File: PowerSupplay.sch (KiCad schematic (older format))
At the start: 26 parts, among them J13 Jack-DC, U4 AP1117-33, U5 MC34063, U6 MC34063, U7 78M09

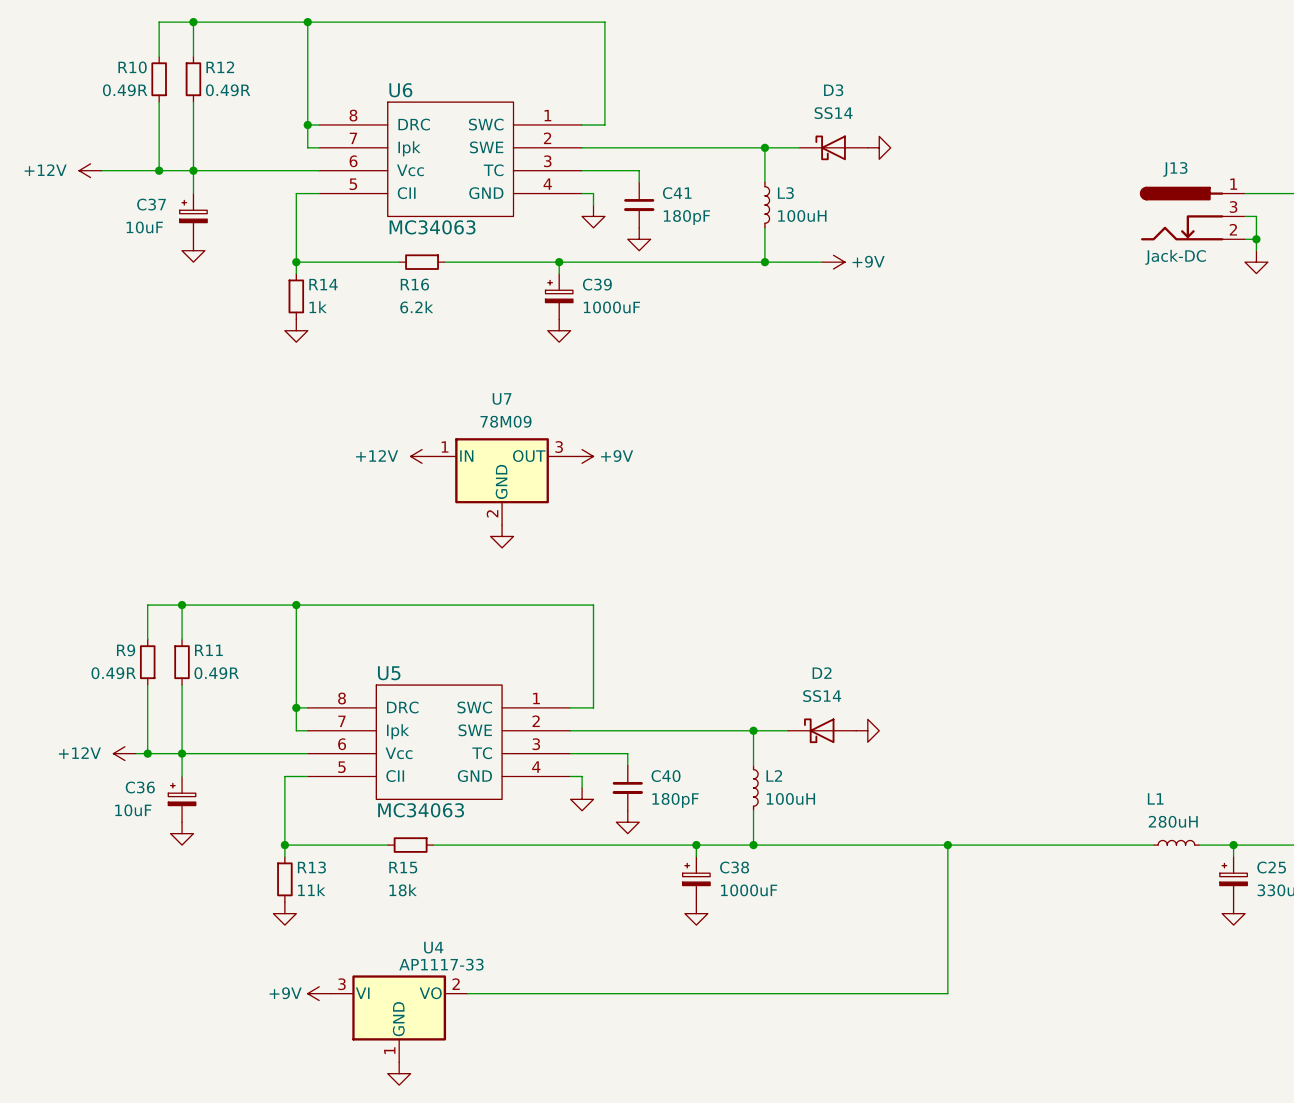
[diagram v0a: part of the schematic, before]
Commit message: TODO: power supplay connector
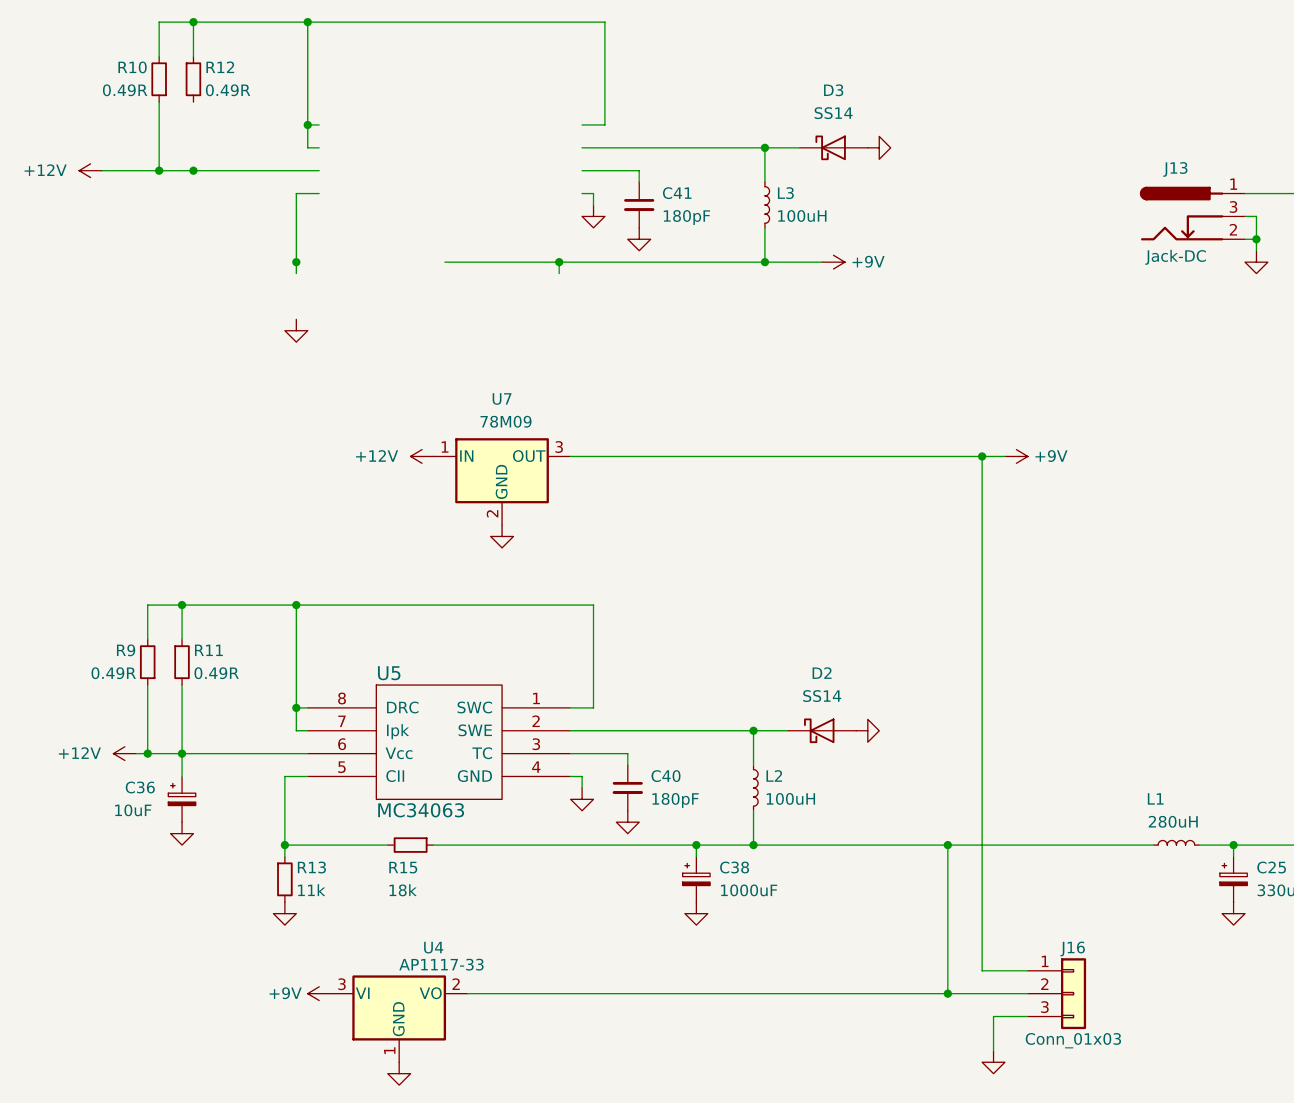
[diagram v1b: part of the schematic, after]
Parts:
- removed C37: 10uF, Capacitors_ThroughHole:CP_Radial_D4.0mm_P2.00mm, symbol CP_Small
- removed C39: 1000uF, Capacitors_ThroughHole:CP_Radial_D10.0mm_P5.00mm, symbol CP_Small
- removed R14: 1k, UI:R_1206_0603, symbol R_Small
- removed R16: 6.2k, UI:R_1206_0603, symbol R_Small
- removed U6: MC34063, UI:SOIC-8_3.9x4.9mm_Pitch1.27mm, symbol MC34063
- added J16: Conn_01x03, symbol Conn_01x03
- C36: footprint Capacitors_ThroughHole:CP_Radial_D4.0mm_P2.00mm -> Capacitors_THT:CP_Radial_D6.3mm_P2.50mm
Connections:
- wire segments 55 -> 58
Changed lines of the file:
@@
 	1250 2000 2200 2000
-Wire Wire Line
-	1650 1700 1650 2100
 Wire Wire Line
 	1650 1500 1650 1350
@@
 Wire Wire Line
 	2750 2400 4400 2400
-Wire Wire Line
-	2550 2400 2100 2400
 Connection ~ 2100 2400
 $Comp
-L GND #PWR052
+L GND #PWR68
 U 1 1 5DD9A087
 P 4600 1900
-F 0 "#PWR052" H 4600 1650 50  0001 C CNN
+F 0 "#PWR68" H 4600 1650 50  0001 C CNN
 F 1 "GND" H 4600 1750 50  0001 C CNN
 F 2 "" H 4600 1900 50  0001 C CNN
@@
 Connection ~ 3250 2400
 $Comp
-L GND #PWR053
+L GND #PWR64
 U 1 1 5DD9A371
 P 3600 2250
-F 0 "#PWR053" H 3600 2000 50  0001 C CNN
+F 0 "#PWR64" H 3600 2000 50  0001 C CNN
 F 1 "GND" H 3600 2100 50  0001 C CNN
 F 2 "" H 3600 2250 50  0001 C CNN
@@
 $EndComp
 $Comp
-L GND #PWR054
+L GND #PWR62
 U 1 1 5DD9A42B
 P 3400 2150
-F 0 "#PWR054" H 3400 1900 50  0001 C CNN
+F 0 "#PWR62" H 3400 1900 50  0001 C CNN
 F 1 "GND" H 3400 2000 50  0001 C CNN
 F 2 "" H 3400 2150 50  0001 C CNN
@@
 Connection ~ 2150 1350
 $Comp
-L +12V #PWR055
+L +12V #PWR52
 U 1 1 5DD9A4E4
 P 1250 2000
-F 0 "#PWR055" H 1250 1850 50  0001 C CNN
+F 0 "#PWR52" H 1250 1850 50  0001 C CNN
 F 1 "+12V" V 1250 2250 50  0000 C CNN
 F 2 "" H 1250 2000 50  0001 C CNN
@@
 Connection ~ 4150 2400
 $Comp
-L +12V #PWR056
+L +12V #PWR59
 U 1 1 5DD9C169
 P 2700 3250
-F 0 "#PWR056" H 2700 3100 50  0001 C CNN
+F 0 "#PWR59" H 2700 3100 50  0001 C CNN
 F 1 "+12V" V 2700 3500 50  0000 C CNN
 F 2 "" H 2700 3250 50  0001 C CNN
@@
 $EndComp
 $Comp
-L +9V #PWR057
+L +9V #PWR66
 U 1 1 5DD9C2C5
 P 4400 2400
-F 0 "#PWR057" H 4400 2250 50  0001 C CNN
+F 0 "#PWR66" H 4400 2250 50  0001 C CNN
 F 1 "+9V" V 4400 2600 50  0000 C CNN
 F 2 "" H 4400 2400 50  0001 C CNN
@@
 $EndComp
 $Comp
-L +9V #PWR058
+L +9V #PWR70
 U 1 1 5DD9C3E9
-P 3300 3250
-F 0 "#PWR058" H 3300 3100 50  0001 C CNN
-F 1 "+9V" V 3300 3450 50  0000 C CNN
-F 2 "" H 3300 3250 50  0001 C CNN
-F 3 "" H 3300 3250 50  0001 C CNN
-	1    3300 3250
+P 5200 3250
+F 0 "#PWR70" H 5200 3100 50  0001 C CNN
+F 1 "+9V" V 5200 3450 50  0000 C CNN
+F 2 "" H 5200 3250 50  0001 C CNN
+F 3 "" H 5200 3250 50  0001 C CNN
+	1    5200 3250
 	0    1    1    0
 $EndComp
 $Comp
-L GND #PWR059
+L GND #PWR60
 U 1 1 5DD9C454
 P 3000 3550
-F 0 "#PWR059" H 3000 3300 50  0001 C CNN
+F 0 "#PWR60" H 3000 3300 50  0001 C CNN
 F 1 "GND" H 3000 3400 50  0001 C CNN
 F 2 "" H 3000 3550 50  0001 C CNN
@@
 $EndComp
 $Comp
-L GND #PWR060
-U 1 1 5DD9C4CE
-P 3250 2650
-F 0 "#PWR060" H 3250 2400 50  0001 C CNN
-F 1 "GND" H 3250 2500 50  0001 C CNN
-F 2 "" H 3250 2650 50  0001 C CNN
-F 3 "" H 3250 2650 50  0001 C CNN
-	1    3250 2650
-	1    0    0    -1
-$EndComp
-$Comp
-L GND #PWR061
+L GND #PWR56
 U 1 1 5DD9C54A
 P 2100 2650
-F 0 "#PWR061" H 2100 2400 50  0001 C CNN
+F 0 "#PWR56" H 2100 2400 50  0001 C CNN
 F 1 "GND" H 2100 2500 50  0001 C CNN
 F 2 "" H 2100 2650 50  0001 C CNN
@@
 	1    0    0    -1
 $EndComp
-$Comp
-L GND #PWR062
-U 1 1 5DD9C5AC
-P 1650 2300
-F 0 "#PWR062" H 1650 2050 50  0001 C CNN
-F 1 "GND" H 1650 2150 50  0001 C CNN
-F 2 "" H 1650 2300 50  0001 C CNN
-F 3 "" H 1650 2300 50  0001 C CNN
-	1    1650 2300
-	1    0    0    -1
-$EndComp
 Wire Wire Line
 	1400 4550 2150 4550
@@
 Connection ~ 2050 4950
 $Comp
-L GND #PWR063
+L GND #PWR67
 U 1 1 5DD9C919
 P 4550 4450
-F 0 "#PWR063" H 4550 4200 50  0001 C CNN
+F 0 "#PWR67" H 4550 4200 50  0001 C CNN
 F 1 "GND" H 4550 4300 50  0001 C CNN
 F 2 "" H 4550 4450 50  0001 C CNN
@@
 	3550 4550 3550 4600
 $Comp
-L GND #PWR064
+L GND #PWR63
 U 1 1 5DD9C936
 P 3550 4800
-F 0 "#PWR064" H 3550 4550 50  0001 C CNN
+F 0 "#PWR63" H 3550 4550 50  0001 C CNN
 F 1 "GND" H 3550 4650 50  0001 C CNN
 F 2 "" H 3550 4800 50  0001 C CNN
@@
 $EndComp
 $Comp
-L GND #PWR065
+L GND #PWR61
 U 1 1 5DD9C93C
 P 3350 4700
-F 0 "#PWR065" H 3350 4450 50  0001 C CNN
+F 0 "#PWR61" H 3350 4450 50  0001 C CNN
 F 1 "GND" H 3350 4550 50  0001 C CNN
 F 2 "" H 3350 4700 50  0001 C CNN
@@
 Connection ~ 4100 4950
 $Comp
-L GND #PWR066
+L GND #PWR58
 U 1 1 5DD9C97A
 P 2550 5900
-F 0 "#PWR066" H 2550 5650 50  0001 C CNN
+F 0 "#PWR58" H 2550 5650 50  0001 C CNN
 F 1 "GND" H 2550 5750 50  0001 C CNN
 F 2 "" H 2550 5900 50  0001 C CNN
@@
 $EndComp
 $Comp
-L GND #PWR067
+L GND #PWR65
 U 1 1 5DD9C980
 P 3850 5200
-F 0 "#PWR067" H 3850 4950 50  0001 C CNN
+F 0 "#PWR65" H 3850 4950 50  0001 C CNN
 F 1 "GND" H 3850 5050 50  0001 C CNN
 F 2 "" H 3850 5200 50  0001 C CNN
@@
 $EndComp
 $Comp
-L GND #PWR068
+L GND #PWR55
 U 1 1 5DD9C98C
 P 2050 5200
-F 0 "#PWR068" H 2050 4950 50  0001 C CNN
+F 0 "#PWR55" H 2050 4950 50  0001 C CNN
 F 1 "GND" H 2050 5050 50  0001 C CNN
 F 2 "" H 2050 5200 50  0001 C CNN
@@
 $EndComp
 $Comp
-L GND #PWR069
+L GND #PWR54
 U 1 1 5DD9C992
 P 1600 4850
-F 0 "#PWR069" H 1600 4600 50  0001 C CNN
+F 0 "#PWR54" H 1600 4600 50  0001 C CNN
 F 1 "GND" H 1600 4700 50  0001 C CNN
 F 2 "" H 1600 4850 50  0001 C CNN
@@
 $EndComp
 $Comp
-L +3V3 #PWR070
+L +3V3 #PWR75
 U 1 1 5DDE50CB
 P 6800 4950
-F 0 "#PWR070" H 6800 4800 50  0001 C CNN
+F 0 "#PWR75" H 6800 4800 50  0001 C CNN
 F 1 "+3V3" V 6800 5200 50  0000 C CNN
 F 2 "" H 6800 4950 50  0001 C CNN
@@
 $EndComp
 $Comp
-L GND #PWR071
+L GND #PWR71
 U 1 1 5DDE5565
 P 6200 5200
-F 0 "#PWR071" H 6200 4950 50  0001 C CNN
+F 0 "#PWR71" H 6200 4950 50  0001 C CNN
 F 1 "GND" H 6200 5050 50  0001 C CNN
 F 2 "" H 6200 5200 50  0001 C CNN
@@
 $EndComp
 $Comp
-L GND #PWR072
+L GND #PWR74
 U 1 1 5DDE5612
 P 6700 5200
-F 0 "#PWR072" H 6700 4950 50  0001 C CNN
+F 0 "#PWR74" H 6700 4950 50  0001 C CNN
 F 1 "GND" H 6700 5050 50  0001 C CNN
 F 2 "" H 6700 5200 50  0001 C CNN
@@
 	6700 5000 6700 4950
 Connection ~ 6700 4950
-$Comp
-L MC34063 U6
-U 1 1 5DDF7FFA
-P 2800 2000
-F 0 "U6" H 2500 2350 60  0000 L CNN
-F 1 "MC34063" H 2500 1750 60  0000 L CNN
-F 2 "UI:SOIC-8_3.9x4.9mm_Pitch1.27mm" H 2700 2000 60  0001 C CNN
-F 3 "" H 2700 2000 60  0000 C CNN
-	1    2800 2000
-	1    0    0    -1
-$EndComp
 $Comp
 L MC34063 U5
@@
 $EndComp
 $Comp
-L CP_Small C39
-U 1 1 5DDF914E
-P 3250 2550
-F 0 "C39" H 3350 2600 50  0000 L CNN
-F 1 "1000uF" H 3350 2500 50  0000 L CNN
-F 2 "Capacitors_ThroughHole:CP_Radial_D10.0mm_P5.00mm" H 3250 2550 50  0001 C CNN
-F 3 "" H 3250 2550 50  0001 C CNN
-	1    3250 2550
-	1    0    0    -1
-$EndComp
-$Comp
-L R_Small R16
-U 1 1 5DDF965B
-P 2650 2400
-F 0 "R16" V 2750 2300 50  0000 L CNN
-F 1 "6.2k" V 2850 2300 50  0000 L CNN
-F 2 "UI:R_1206_0603" H 2650 2400 50  0001 C CNN
-F 3 "" H 2650 2400 50  0001 C CNN
-	1    2650 2400
-	0    1    1    0
-$EndComp
-$Comp
-L R_Small R14
-U 1 1 5DDF97A0
-P 2100 2550
-F 0 "R14" H 2150 2600 50  0000 L CNN
-F 1 "1k" H 2150 2500 50  0000 L CNN
-F 2 "UI:R_1206_0603" H 2100 2550 50  0001 C CNN
-F 3 "" H 2100 2550 50  0001 C CNN
-	1    2100 2550
-	1    0    0    -1
-$EndComp
-$Comp
-L CP_Small C37
-U 1 1 5DDF9926
-P 1650 2200
-F 0 "C37" H 1400 2250 50  0000 L CNN
-F 1 "10uF" H 1350 2150 50  0000 L CNN
-F 2 "Capacitors_ThroughHole:CP_Radial_D4.0mm_P2.00mm" H 1650 2200 50  0001 C CNN
-F 3 "" H 1650 2200 50  0001 C CNN
-	1    1650 2200
-	1    0    0    -1
-$EndComp
-$Comp
 L L_Small L3
 U 1 1 5DDFA0D4
@@
 F 0 "C36" H 1350 4800 50  0000 L CNN
 F 1 "10uF" H 1300 4700 50  0000 L CNN
-F 2 "Capacitors_ThroughHole:CP_Radial_D4.0mm_P2.00mm" H 1600 4750 50  0001 C CNN
+F 2 "Capacitors_THT:CP_Radial_D6.3mm_P2.50mm" H 1600 4750 50  0001 C CNN
 F 3 "" H 1600 4750 50  0001 C CNN
 	1    1600 4750
@@
 $EndComp
 $Comp
-L +9V #PWR073
+L +9V #PWR57
 U 1 1 5DE21DEE
 P 2250 5600
-F 0 "#PWR073" H 2250 5450 50  0001 C CNN
+F 0 "#PWR57" H 2250 5450 50  0001 C CNN
 F 1 "+9V" V 2250 5800 50  0000 C CNN
 F 2 "" H 2250 5600 50  0001 C CNN
@@
 $EndComp
 $Comp
-L +12V #PWR074
+L +12V #PWR53
 U 1 1 5E97FA32
 P 1400 4550
-F 0 "#PWR074" H 1400 4400 50  0001 C CNN
+F 0 "#PWR53" H 1400 4400 50  0001 C CNN
 F 1 "+12V" V 1400 4800 50  0000 C CNN
 F 2 "" H 1400 4550 50  0001 C CNN
@@
 Connection ~ 3850 4950
 Wire Wire Line
-	2850 5600 4950 5600
-Wire Wire Line
-	4950 5600 4950 4950
+	4950 4950 4950 5600
 Connection ~ 4950 4950
 $Comp
@@
 $EndComp
 $Comp
-L +12V #PWR075
+L +12V #PWR73
 U 1 1 5E994C0D
 P 6500 2100
-F 0 "#PWR075" H 6500 1950 50  0001 C CNN
+F 0 "#PWR73" H 6500 1950 50  0001 C CNN
 F 1 "+12V" V 6500 2350 50  0000 C CNN
 F 2 "" H 6500 2100 50  0001 C CNN
@@
 	6250 2100 6500 2100
 $Comp
-L GND #PWR076
+L GND #PWR72
 U 1 1 5E994E36
 P 6300 2350
-F 0 "#PWR076" H 6300 2100 50  0001 C CNN
+F 0 "#PWR72" H 6300 2100 50  0001 C CNN
 F 1 "GND" H 6300 2200 50  0001 C CNN
 F 2 "" H 6300 2350 50  0001 C CNN
@@
 	6250 2300 6300 2300
 Connection ~ 6300 2300
+Wire Wire Line
+	2850 5600 5300 5600
+Connection ~ 4950 5600
+Wire Wire Line
+	3300 3250 5200 3250
+Wire Wire Line
+	5100 3250 5100 5500
+Wire Wire Line
+	5100 5500 5300 5500
+Connection ~ 5100 3250
+$Comp
+L GND #PWR69
+U 1 1 5E9B2413
+P 5150 5850
+F 0 "#PWR69" H 5150 5600 50  0001 C CNN
+F 1 "GND" H 5150 5700 50  0001 C CNN
+F 2 "" H 5150 5850 50  0001 C CNN
+F 3 "" H 5150 5850 50  0001 C CNN
+	1    5150 5850
+	1    0    0    -1
+$EndComp
+Wire Wire Line
+	5150 5850 5150 5700
+Wire Wire Line
+	5150 5700 5300 5700
+$Comp
+L Conn_01x03 J16
+U 1 1 5E9B250C
+P 5500 5600
+F 0 "J16" H 5500 5800 50  0000 C CNN
+F 1 "Conn_01x03" H 5500 5400 50  0000 C CNN
+F 2 "" H 5500 5600 50  0001 C CNN
+F 3 "" H 5500 5600 50  0001 C CNN
+	1    5500 5600
+	1    0    0    -1
+$EndComp
 $EndSCHEMATC
